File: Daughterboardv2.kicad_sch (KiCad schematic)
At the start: 15 parts, among them J1 Conn_01x06_Male, J2 Conn_01x01, J3 Conn_01x05_Pin, J4 Conn_01x05_Pin, U1 XIAO-ESP32C3, U2 TJA1042T-3

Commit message: add second option for CAN transorb
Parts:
- added D2: PESD1CAN, Package_TO_SOT_SMD:SOT-23, symbol Device:D_TVS_Dual_AAC
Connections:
- net CANH: now also D2.1 (A1)
- net CANL: now also D2.2 (A2)
- net GND: now also D2.3 (common)
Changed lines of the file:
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@@
   (junction (at 63.246 52.832) (diameter 0) (color 0 0 0 0)
   )
+  (junction (at 60.071 72.263) (diameter 0) (color 0 0 0 0)
+  )
   (junction (at 64.008 55.88) (diameter 0) (color 0 0 0 0)
   )
@@
   (junction (at 171.958 53.34) (diameter 0) (color 0 0 0 0)
   )
+  (junction (at 62.865 74.803) (diameter 0) (color 0 0 0 0)
+  )
   (junction (at 68.834 46.99) (diameter 0) (color 0 0 0 0)
   )
@@
     (stroke (width 0) (type default))
   )
+  (wire (pts (xy 60.071 72.263) (xy 64.008 72.263))
+    (stroke (width 0) (type default))
+  )
   (wire (pts (xy 134.62 72.39) (xy 134.62 66.04))
     (stroke (width 0) (type default))
@@
     (stroke (width 0) (type default))
   )
+  (wire (pts (xy 62.865 86.106) (xy 62.865 74.803))
+    (stroke (width 0) (type default))
+  )
   (wire (pts (xy 73.66 55.88) (xy 64.008 55.88))
     (stroke (width 0) (type default))
@@
     (stroke (width 0) (type default))
   )
+  (wire (pts (xy 40.005 81.026) (xy 40.005 86.106))
+    (stroke (width 0) (type default))
+  )
   (wire (pts (xy 175.514 50.8) (xy 181.61 50.8))
     (stroke (width 0) (type default))
@@
     (stroke (width 0) (type default))
   )
+  (wire (pts (xy 57.785 86.106) (xy 62.865 86.106))
+    (stroke (width 0) (type default))
+  )
   (wire (pts (xy 89.408 57.912) (xy 89.408 60.96))
     (stroke (width 0) (type default))
   )
+  (wire (pts (xy 62.865 74.803) (xy 65.278 74.803))
+    (stroke (width 0) (type default))
+  )
   (wire (pts (xy 93.98 55.88) (xy 73.66 55.88))
     (stroke (width 0) (type default))
@@
     (stroke (width 0) (type default))
   )
+  (wire (pts (xy 60.071 81.026) (xy 60.071 72.263))
+    (stroke (width 0) (type default))
+  )
   (wire (pts (xy 61.722 50.292) (xy 74.422 50.292))
     (stroke (width 0) (type default))
@@
     (stroke (width 0) (type default))
   )
-  (wire (pts (xy 57.912 74.803) (xy 65.278 74.803))
+  (wire (pts (xy 57.912 74.803) (xy 62.865 74.803))
     (stroke (width 0) (type default))
   )
@@
     (stroke (width 0) (type default))
   )
+  (wire (pts (xy 40.005 81.026) (xy 60.071 81.026))
+    (stroke (width 0) (type default))
+  )
   (wire (pts (xy 162.052 48.768) (xy 162.052 50.8))
     (stroke (width 0) (type default))
@@
     (stroke (width 0) (type default))
   )
+  (wire (pts (xy 48.895 89.916) (xy 48.895 91.059))
+    (stroke (width 0) (type default))
+  )
   (wire (pts (xy 65.278 74.803) (xy 65.278 57.912))
     (stroke (width 0) (type default))
@@
     (stroke (width 0) (type default))
   )
-  (wire (pts (xy 57.912 72.263) (xy 64.008 72.263))
+  (wire (pts (xy 57.912 72.263) (xy 60.071 72.263))
     (stroke (width 0) (type default))
   )
@@
         (path "/2cafaedd-8bd5-41d3-b750-dd0af036224e"
           (reference "#PWR09") (unit 1)
+        )
+      )
+    )
+  )
+  (symbol (lib_id "power:GND") (at 48.895 91.059 0) (unit 1)
+    (in_bom yes) (on_board yes) (dnp no) (fields_autoplaced)
+    (property "Reference" "#PWR019" (at 48.895 97.409 0)
+      (effects (font (size 1.27 1.27)) hide)
+    )
+    (property "Value" "GND" (at 48.895 95.1921 0)
+      (effects (font (size 1.27 1.27)))
+    )
+    (property "Footprint" "" (at 48.895 91.059 0)
+      (effects (font (size 1.27 1.27)) hide)
+    )
+    (property "Datasheet" "" (at 48.895 91.059 0)
+      (effects (font (size 1.27 1.27)) hide)
+    )
+    (pin "1")
+    (instances
+      (project "Daughterboardv2"
+        (path "/2cafaedd-8bd5-41d3-b750-dd0af036224e"
+          (reference "#PWR019") (unit 1)
         )
       )
@@
         )
       )
+    )
+  )
+  (symbol (lib_id "Device:D_TVS_Dual_AAC") (at 48.895 86.106 0) (unit 1)
+    (in_bom yes) (on_board yes) (dnp no)
+    (property "Reference" "D2" (at 48.895 80.6917 0)
+      (effects (font (size 1.27 1.27)))
+    )
+    (property "Value" "PESD1CAN" (at 54.737 90.17 0)
+      (effects (font (size 1.27 1.27)))
+    )
+    (property "Footprint" "Package_TO_SOT_SMD:SOT-23" (at 45.085 86.106 0)
+      (effects (font (size 1.27 1.27)) hide)
+    )
+    (property "Datasheet" "~" (at 45.085 86.106 0)
+      (effects (font (size 1.27 1.27)) hide)
+    )
+    (pin "2")
+    (pin "3")
+    (pin "1")
+    (instances
+      (project "Daughterboardv2"
+        (path "/2cafaedd-8bd5-41d3-b750-dd0af036224e"
+          (reference "D2") (unit 1)
+        )
+      )

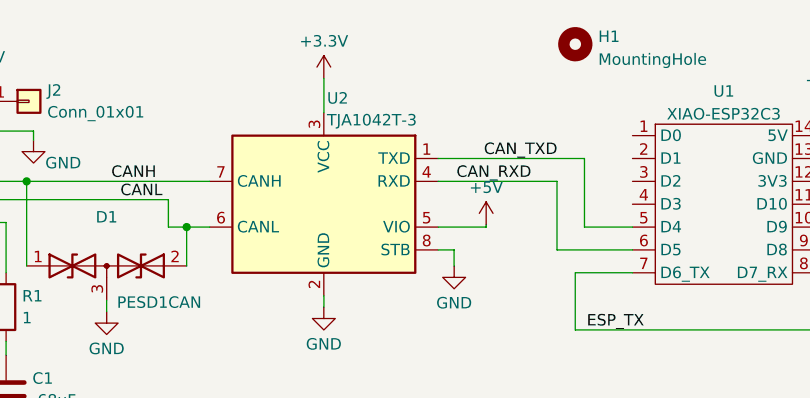
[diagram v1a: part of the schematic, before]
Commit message: schematic and pcb bug fix for Vcc and Vio swap on CAN xcvr
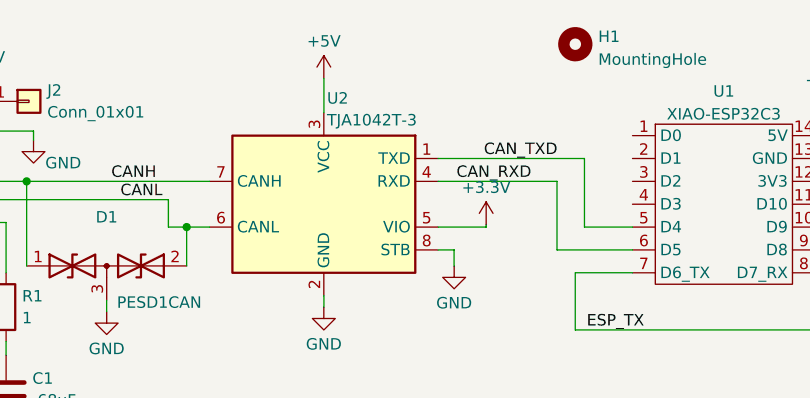
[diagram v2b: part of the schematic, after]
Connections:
- net +3.3V: now also U2.5 (VIO); no longer U2.3 (VCC)
- net +5V: now also U2.3 (VCC); no longer U2.5 (VIO)
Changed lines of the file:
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@@
-    )
-  )
-  (symbol (lib_id "power:+5V") (at 124.714 60.706 0) (unit 1)
-    (in_bom yes) (on_board yes) (dnp no) (fields_autoplaced)
-    (property "Reference" "#PWR07" (at 124.714 64.516 0)
-      (effects (font (size 1.27 1.27)) hide)
-    )
-    (property "Value" "+5V" (at 124.714 56.5729 0)
-      (effects (font (size 1.27 1.27)))
-    )
-    (property "Footprint" "" (at 124.714 60.706 0)
-      (effects (font (size 1.27 1.27)) hide)
-    )
-    (property "Datasheet" "" (at 124.714 60.706 0)
-      (effects (font (size 1.27 1.27)) hide)
-    )
-    (pin "1")
-    (instances
-      (project "Daughterboardv2"
-        (path "/2cafaedd-8bd5-41d3-b750-dd0af036224e"
-          (reference "#PWR07") (unit 1)
-        )
-      )
     )
   )
@@
     )
   )
+  (symbol (lib_id "power:+5V") (at 106.68 44.45 0) (unit 1)
+    (in_bom yes) (on_board yes) (dnp no) (fields_autoplaced)
+    (property "Reference" "#PWR07" (at 106.68 48.26 0)
+      (effects (font (size 1.27 1.27)) hide)
+    )
+    (property "Value" "+5V" (at 106.68 40.3169 0)
+      (effects (font (size 1.27 1.27)))
+    )
+    (property "Footprint" "" (at 106.68 44.45 0)
+      (effects (font (size 1.27 1.27)) hide)
+    )
+    (property "Datasheet" "" (at 106.68 44.45 0)
+      (effects (font (size 1.27 1.27)) hide)
+    )
+    (pin "1")
+    (instances
+      (project "Daughterboardv2"
+        (path "/2cafaedd-8bd5-41d3-b750-dd0af036224e"
+          (reference "#PWR07") (unit 1)
+        )
+      )
+    )
+  )
   (symbol (lib_id "power:+12V") (at 68.834 46.228 0) (unit 1)
     (in_bom yes) (on_board yes) (dnp no) (fields_autoplaced)
@@
         (path "/2cafaedd-8bd5-41d3-b750-dd0af036224e"
           (reference "#PWR09") (unit 1)
+        )
+      )
+    )
+  )
+  (symbol (lib_id "power:+3.3V") (at 124.714 60.706 0) (unit 1)
+    (in_bom yes) (on_board yes) (dnp no) (fields_autoplaced)
+    (property "Reference" "#PWR06" (at 124.714 64.516 0)
+      (effects (font (size 1.27 1.27)) hide)
+    )
+    (property "Value" "+3.3V" (at 124.714 56.5729 0)
+      (effects (font (size 1.27 1.27)))
+    )
+    (property "Footprint" "" (at 124.714 60.706 0)
+      (effects (font (size 1.27 1.27)) hide)
+    )
+    (property "Datasheet" "" (at 124.714 60.706 0)
+      (effects (font (size 1.27 1.27)) hide)
+    )
+    (pin "1")
+    (instances
+      (project "Daughterboardv2"
+        (path "/2cafaedd-8bd5-41d3-b750-dd0af036224e"
+          (reference "#PWR06") (unit 1)
         )
       )
@@
         )
       )
-    )
-  )
-  (symbol (lib_id "power:+3.3V") (at 106.68 44.45 0) (unit 1)
-    (in_bom yes) (on_board yes) (dnp no) (fields_autoplaced)
-    (property "Reference" "#PWR06" (at 106.68 48.26 0)
-      (effects (font (size 1.27 1.27)) hide)
-    )
-    (property "Value" "+3.3V" (at 106.68 40.3169 0)
-      (effects (font (size 1.27 1.27)))
-    )
-    (property "Footprint" "" (at 106.68 44.45 0)
-      (effects (font (size 1.27 1.27)) hide)
-    )
-    (property "Datasheet" "" (at 106.68 44.45 0)
-      (effects (font (size 1.27 1.27)) hide)
-    )
-    (pin "1")
-    (instances
-      (project "Daughterboardv2"
-        (path "/2cafaedd-8bd5-41d3-b750-dd0af036224e"
-          (reference "#PWR06") (unit 1)
-        )
-      )
